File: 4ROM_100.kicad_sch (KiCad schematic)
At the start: 7 parts, among them J1 Tandy_100_102_200_option_rom, J2 4ROM_prog_female, U1 SST39SF010A

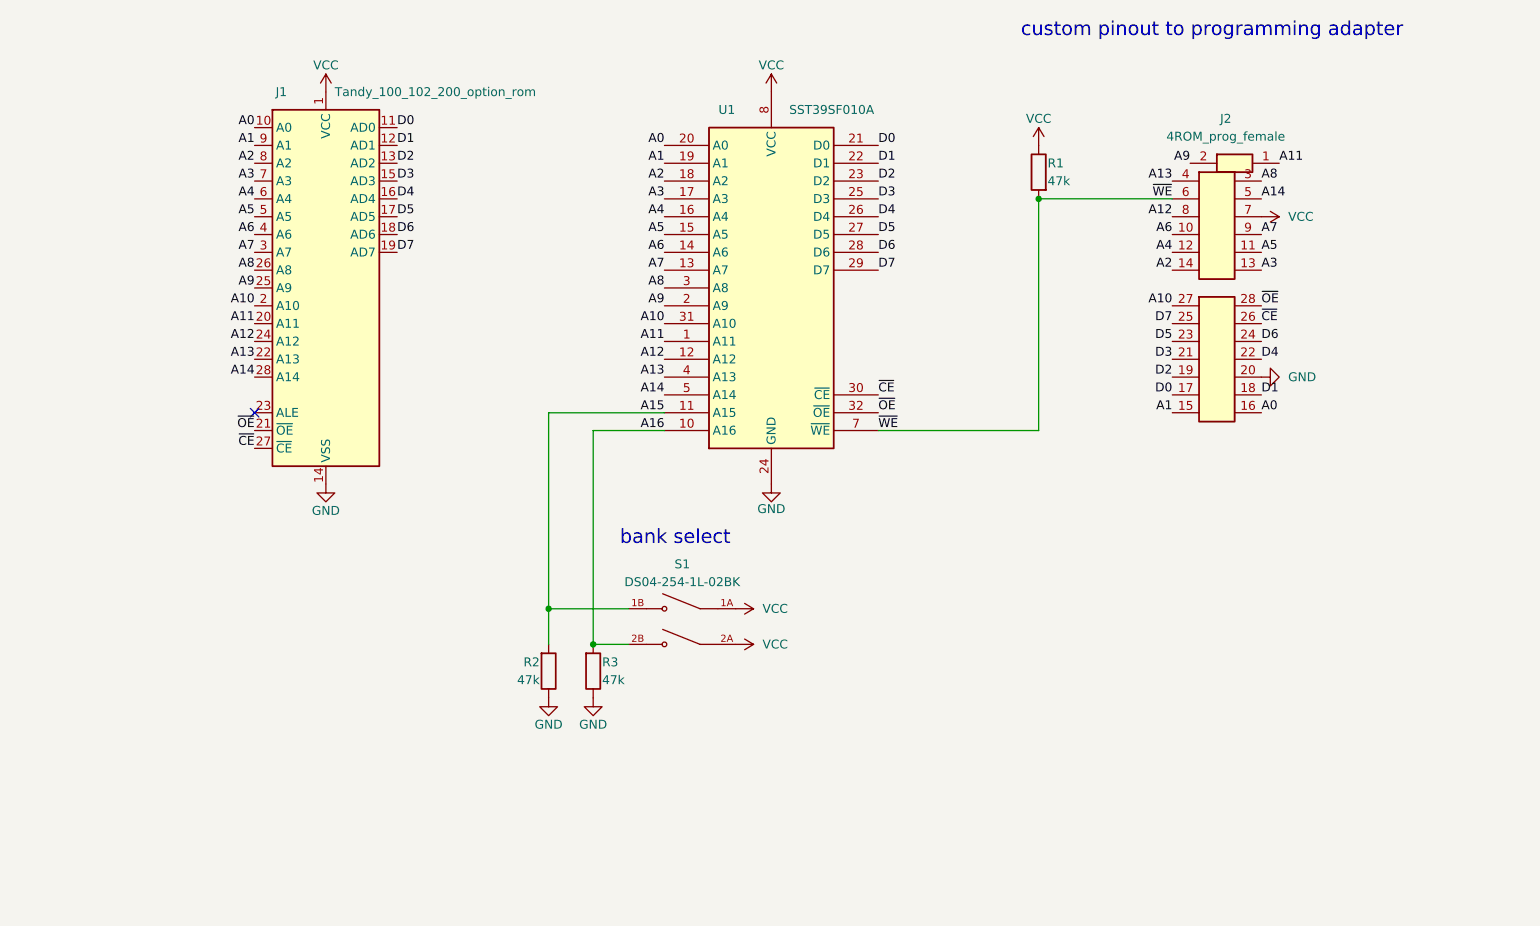
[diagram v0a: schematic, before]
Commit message: 4ROM_78802 and programming adapter are now tested and verified
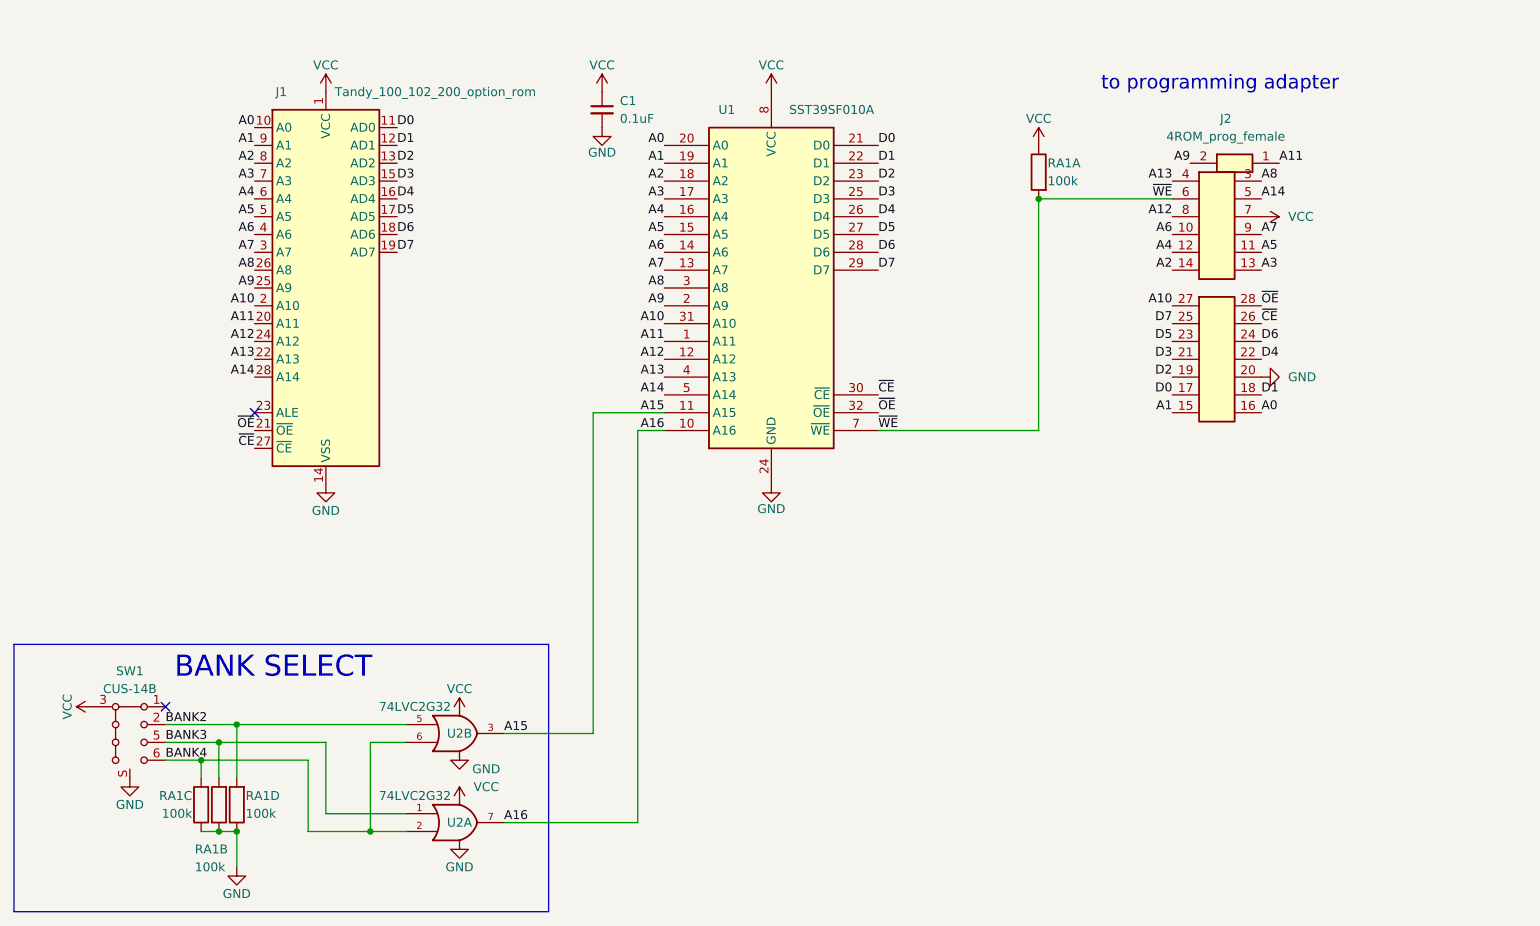
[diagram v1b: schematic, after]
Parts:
- removed R1, R2, R3: 47k, 000_LOCAL:R_0805, symbol 000_LOCAL:R
- removed S1: DS04-254-1L-02BK, 000_LOCAL:SW_DS04-254-1L-02BK, symbol 000_LOCAL:DS04-254-1L-02BK
- added C1: 0.1uF, 000_LOCAL:C_0805, symbol 000_LOCAL:C
- added RA1: 100k, 000_LOCAL:R_Array_Convex_4x0612, symbol 000_LOCAL:R_Array_04
- added SW1: CUS-14B, 000_LOCAL:SW_SP4T_CUS-14B, symbol 000_LOCAL:SW_1P4T_CUS-14B
- added U2: 74LVC2G32, 000_LOCAL:TSSOP-8_3x3mm_P0.65mm, symbol 000_LOCAL:74LVC2G32
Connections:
- net A15: now also U2.3
- net A16: now also U2.7
- net GND: now also C1.2, RA1.5 (R4.2), RA1.6 (R3.2), RA1.7 (R2.2), SW1.S, U2.4 (GND), U2.4 (GND)
- net VCC: now also C1.1, RA1.8 (R1.2), SW1.3 (C), SW1.4 (C), U2.8 (VCC), U2.8 (VCC)
- net ~{WE}: now also RA1.1 (R1.1)
- new net BANK2: RA1.4 (R4.1), SW1.2, U2.5
- new net BANK3: RA1.2 (R2.1), SW1.5, U2.1
- new net BANK4: RA1.3 (R3.1), SW1.6, U2.2, U2.6
- no-connect marks 1 -> 2
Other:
- note added: "BANK SELECT"
- note added: "to programming adapter"
- note removed: "bank select"
- note removed: "custom pinout to programming adapter"

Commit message: cosmetic schematic touchups
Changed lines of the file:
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@@
       (effects (font (size 1.27 1.27)) hide)
     )
-    (property "Value" "VCC" (id 1) (at 52.07 148.59 0))
+    (property "Value" "VCC" (id 1) (at 50.8 148.59 90))
     (property "Footprint" "" (id 2) (at 55.88 148.59 0)
       (effects (font (size 1.27 1.27)) hide)
@@
     (pin "6")
   )
-  (symbol (lib_id "000_LOCAL:VCC") (at 107.95 149.86 0) (mirror y) (unit 1)
-    (in_bom yes) (on_board yes)
-    (property "Reference" "#PWR0109" (id 0) (at 107.95 153.67 0)
-      (effects (font (size 1.27 1.27)) hide)
-    )
-    (property "Value" "VCC" (id 1) (at 107.95 146.05 0))
-    (property "Footprint" "" (id 2) (at 107.95 149.86 0)
-      (effects (font (size 1.27 1.27)) hide)
-    )
-    (property "Datasheet" "" (id 3) (at 107.95 149.86 0)
-      (effects (font (size 1.27 1.27)) hide)
-    )
-    (pin "1")
-  )
   (symbol (lib_id "000_LOCAL:C") (at 128.27 63.5 0) (unit 1)
     (in_bom yes) (on_board yes) (fields_autoplaced)
@@
     (pin "2")
   )
-  (symbol (lib_id "000_LOCAL:GND") (at 107.95 167.64 0) (mirror y) (unit 1)
-    (in_bom yes) (on_board yes)
-    (property "Reference" "#PWR0112" (id 0) (at 107.95 171.45 0)
-      (effects (font (size 1.27 1.27)) hide)
-    )
-    (property "Value" "GND" (id 1) (at 107.95 171.45 0))
-    (property "Footprint" "" (id 2) (at 107.95 167.64 0)
-      (effects (font (size 1.27 1.27)) hide)
-    )
-    (property "Datasheet" "" (id 3) (at 107.95 167.64 0)
-      (effects (font (size 1.27 1.27)) hide)
-    )
-    (pin "1")
-  )
   (symbol (lib_id "000_LOCAL:R_Array_04") (at 190.5 72.39 0) (mirror x) (unit 1)
     (in_bom yes) (on_board yes)
@@
     (pin "4")
     (pin "5")
-  )
-  (symbol (lib_id "000_LOCAL:VCC") (at 107.95 162.56 0) (mirror y) (unit 1)
-    (in_bom yes) (on_board yes)
-    (property "Reference" "#PWR0113" (id 0) (at 107.95 166.37 0)
-      (effects (font (size 1.27 1.27)) hide)
-    )
-    (property "Value" "VCC" (id 1) (at 111.76 160.02 0))
-    (property "Footprint" "" (id 2) (at 107.95 162.56 0)
-      (effects (font (size 1.27 1.27)) hide)
-    )
-    (property "Datasheet" "" (id 3) (at 107.95 162.56 0)
-      (effects (font (size 1.27 1.27)) hide)
-    )
-    (pin "1")
-  )
-  (symbol (lib_id "000_LOCAL:GND") (at 107.95 154.94 0) (mirror y) (unit 1)
-    (in_bom yes) (on_board yes)
-    (property "Reference" "#PWR0114" (id 0) (at 107.95 158.75 0)
-      (effects (font (size 1.27 1.27)) hide)
-    )
-    (property "Value" "GND" (id 1) (at 111.76 157.48 0))
-    (property "Footprint" "" (id 2) (at 107.95 154.94 0)
-      (effects (font (size 1.27 1.27)) hide)
-    )
-    (property "Datasheet" "" (id 3) (at 107.95 154.94 0)
-      (effects (font (size 1.27 1.27)) hide)
-    )
-    (pin "1")
   )
   (symbol (lib_id "power:VCC") (at 222.25 78.74 270) (unit 1)
@@
       (reference "#PWR0108") (unit 1) (value "GND") (footprint "")
     )
-    (path "/6b889fda-5121-4429-8c0c-e4348c25d886"
-      (reference "#PWR0109") (unit 1) (value "VCC") (footprint "")
-    )
     (path "/bfb01695-8269-426c-a716-e41efe9a2b4b"
       (reference "#PWR0110") (unit 1) (value "VCC") (footprint "")
@@
       (reference "#PWR0111") (unit 1) (value "GND") (footprint "")
     )
-    (path "/8afd2988-a17a-4d43-8fed-e0ebadad3ed2"
-      (reference "#PWR0112") (unit 1) (value "GND") (footprint "")
-    )
-    (path "/a8afa69e-92b1-41c9-ba5b-7942a1bea764"
-      (reference "#PWR0113") (unit 1) (value "VCC") (footprint "")
-    )
-    (path "/bde976a5-824f-4b3f-b5b1-0ce8548a4316"
-      (reference "#PWR0114") (unit 1) (value "GND") (footprint "")
-    )
     (path "/239cc396-579f-4eff-89b9-b75422b61f53"
